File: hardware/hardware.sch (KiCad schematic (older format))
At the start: 18 parts, among them Q1 BUK7M33-60EX, U1 Teensy4.1_DEV-16771, U2 LT1910, U3 OKI, U4 OKI-78SR-3.3_1.5-W36H-C

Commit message: Board Review
Thermistor moved
Edit Ethernet
Find nichrome wire to be used before PDR
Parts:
- added C?: C_Small, symbol Device:C_Small
- added J?: RJ45_LED_Shielded, symbol Connector:RJ45_LED_Shielded
- added J?: 6P6C, symbol Connector:6P6C
- added TP? (x2): TestPoint, symbol Connector:TestPoint
- Conn1: symbol MRDT_Connectors:AndersonPP -> hardware-rescue:AndersonPP-MRDT_Connectors
- U2: symbol MRDT_ICs:LT1910 -> hardware-rescue:LT1910-MRDT_ICs
- U3: symbol MRDT_Devices:OKI -> hardware-rescue:OKI-MRDT_Devices
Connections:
- net labels added: EthernetMadness
- wire segments 84 -> 108
- no-connect marks 51 -> 56
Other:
- note removed: "A17 / A16 = TH1 / (TH1 + Nichrome Resistance)"
- note removed: "ethernet connection to teensy"
- moved on the sheet: TH1
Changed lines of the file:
@@
 $EndDescr
 $Comp
-L MRDT_Connectors:AndersonPP Conn1
+L hardware-rescue:AndersonPP-MRDT_Connectors Conn1
 U 4 1 614D2045
 P 700 1600
@@
 $EndComp
 $Comp
-L MRDT_Connectors:AndersonPP Conn1
+L hardware-rescue:AndersonPP-MRDT_Connectors Conn1
 U 1 1 614D689F
 P 700 1000
@@
 	1200 2100 1200 1900
 $Comp
-L MRDT_ICs:LT1910 U2
+L hardware-rescue:LT1910-MRDT_ICs U2
 U 1 1 61539417
 P 2250 1350
@@
 Wire Wire Line
 	2650 2150 2650 2000
-$Comp
-L power:GND #PWR06
-U 1 1 61591C99
-P 5050 6700
-F 0 "#PWR06" H 5050 6450 50  0001 C CNN
-F 1 "GND" V 5055 6572 50  0000 R CNN
-F 2 "" H 5050 6700 50  0001 C CNN
-F 3 "" H 5050 6700 50  0001 C CNN
-	1    5050 6700
-	0    -1   -1   0
-$EndComp
-Wire Wire Line
-	5050 6700 4950 6700
 Wire Wire Line
 	1650 1100 2050 1100
-Connection ~ 3300 2000
 NoConn ~ 4850 3100
 NoConn ~ 4850 3200
@@
 L Device:Thermistor_NTC TH1
 U 1 1 615942DB
-P 6300 2350
-F 0 "TH1" V 6010 2350 50  0000 C CNN
-F 1 "Thermistor_NTC" V 6101 2350 50  0000 C CNN
-F 2 "" H 6300 2400 50  0001 C CNN
-F 3 "~" H 6300 2400 50  0001 C CNN
-	1    6300 2350
+P 5700 1950
+F 0 "TH1" V 5410 1950 50  0000 C CNN
+F 1 "Thermistor_NTC" V 5501 1950 50  0000 C CNN
+F 2 "" H 5700 2000 50  0001 C CNN
+F 3 "~" H 5700 2000 50  0001 C CNN
+	1    5700 1950
 	0    1    1    0
 $EndComp
 Wire Wire Line
-	3300 2000 3300 2350
-Text Notes 7000 2200 0    50   ~ 0
-nichrome connection point
-Wire Wire Line
 	5250 2600 1650 2600
 Wire Wire Line
@@
 Wire Wire Line
 	4950 6800 4950 6700
-Connection ~ 4950 6700
 Wire Wire Line
 	4950 6700 4850 6700
-Text Notes 1550 4100 0    50   ~ 0
-ethernet connection to teensy
-Wire Wire Line
-	3250 3900 1950 3900
-$Comp
-L MRDT_Devices:OKI U3
+$Comp
+L hardware-rescue:OKI-MRDT_Devices U3
 U 1 1 615CF578
 P 6800 3300
@@
 Wire Wire Line
 	7300 4850 7550 4850
-Wire Wire Line
-	3950 1950 5450 1950
 NoConn ~ 3250 5700
 $Comp
@@
 $EndComp
 Wire Wire Line
-	6450 2350 6650 2350
-Connection ~ 6650 2350
-Wire Wire Line
-	6650 2350 7450 2350
-Wire Wire Line
 	5250 4400 5250 2600
 Wire Wire Line
 	4850 4400 5250 4400
 Wire Wire Line
-	4850 5700 5450 5700
-Wire Wire Line
-	5450 1950 5450 5700
-Wire Wire Line
-	3300 2350 6150 2350
-Connection ~ 5450 1950
-Wire Wire Line
-	5450 1950 7150 1950
-Wire Wire Line
 	4850 5800 5650 5800
 Wire Wire Line
-	5650 5800 5650 2600
-Wire Wire Line
-	6650 2350 6650 2600
-Wire Wire Line
-	5650 2600 6650 2600
-Text Notes 6050 1850 0    47   ~ 0
-A17 / A16 = TH1 / (TH1 + Nichrome Resistance)
+	5650 5800 5650 2250
+Wire Wire Line
+	5650 2250 6650 2250
 $Comp
 L Device:Thermistor_NTC TH3
@@
 Wire Wire Line
 	1200 1500 1200 1600
+$Comp
+L Connector:TestPoint TP?
+U 1 1 6164E01B
+P 7150 1950
+F 0 "TP?" V 7104 2138 50  0000 L CNN
+F 1 "TestPoint" V 7195 2138 50  0000 L CNN
+F 2 "" H 7350 1950 50  0001 C CNN
+F 3 "~" H 7350 1950 50  0001 C CNN
+	1    7150 1950
+	0    1    1    0
+$EndComp
+$Comp
+L Connector:TestPoint TP?
+U 1 1 616506C1
+P 7450 2350
+F 0 "TP?" V 7404 2538 50  0000 L CNN
+F 1 "TestPoint" V 7495 2538 50  0000 L CNN
+F 2 "" H 7650 2350 50  0001 C CNN
+F 3 "~" H 7650 2350 50  0001 C CNN
+	1    7450 2350
+	0    1    1    0
+$EndComp
+$Comp
+L Connector:RJ45_LED_Shielded J?
+U 1 1 61651929
+P 1100 4550
+F 0 "J?" V 1054 5080 50  0000 L CNN
+F 1 "RJ45_LED_Shielded" V 1145 5080 50  0000 L CNN
+F 2 "" V 1100 4575 50  0001 C CNN
+F 3 "~" V 1100 4575 50  0001 C CNN
+	1    1100 4550
+	0    1    1    0
+$EndComp
+NoConn ~ 3250 3900
+$Comp
+L Connector:6P6C J?
+U 1 1 61663DF2
+P 1000 5750
+F 0 "J?" V 1103 6180 50  0000 L CNN
+F 1 "6P6C" V 1012 6180 50  0000 L CNN
+F 2 "" V 1000 5775 50  0001 C CNN
+F 3 "~" V 1000 5775 50  0001 C CNN
+	1    1000 5750
+	0    1    -1   0
+$EndComp
+Wire Wire Line
+	1300 4950 1300 5150
+Wire Wire Line
+	600  4550 600  4800
+$Comp
+L power:GND #PWR?
+U 1 1 6167F4AF
+P 600 4800
+F 0 "#PWR?" H 600 4550 50  0001 C CNN
+F 1 "GND" H 605 4627 50  0000 C CNN
+F 2 "" H 600 4800 50  0001 C CNN
+F 3 "" H 600 4800 50  0001 C CNN
+	1    600  4800
+	1    0    0    -1
+$EndComp
+$Comp
+L Device:C_Small C?
+U 1 1 616800CF
+P 1650 5150
+F 0 "C?" H 1742 5196 50  0000 L CNN
+F 1 "C_Small" H 1742 5105 50  0000 L CNN
+F 2 "" H 1650 5150 50  0001 C CNN
+F 3 "~" H 1650 5150 50  0001 C CNN
+	1    1650 5150
+	1    0    0    -1
+$EndComp
+Wire Wire Line
+	1300 5150 1200 5150
+Wire Wire Line
+	1650 5050 1650 5000
+Wire Wire Line
+	800  4950 800  5350
+Wire Wire Line
+	1000 5250 1000 5350
+Wire Wire Line
+	1200 5150 1200 5350
+Wire Wire Line
+	1300 5200 1300 5350
+Wire Wire Line
+	1000 5250 1500 5250
+Wire Wire Line
+	1650 5000 1200 5000
+Wire Wire Line
+	1200 5000 1200 4950
+Connection ~ 1200 5000
+Wire Wire Line
+	900  4950 900  5000
+Wire Wire Line
+	900  5000 1200 5000
+Wire Wire Line
+	1300 5200 1100 5200
+Wire Wire Line
+	1100 5200 1100 4950
+Wire Wire Line
+	900  5350 900  5050
+Wire Wire Line
+	900  5050 1000 5050
+Wire Wire Line
+	1000 5050 1000 4950
+Wire Wire Line
+	1100 5350 1100 5300
+Wire Wire Line
+	1100 5300 1850 5300
+Wire Wire Line
+	1850 5300 1850 4150
+Wire Wire Line
+	1850 4150 1500 4150
+Wire Wire Line
+	1400 4150 1400 4100
+Wire Wire Line
+	1400 4100 1950 4100
+Wire Wire Line
+	1950 4100 1950 5250
+Wire Wire Line
+	1950 5250 1650 5250
+Connection ~ 1650 5250
+Wire Wire Line
+	1500 4950 1500 5250
+Connection ~ 1500 5250
+Wire Wire Line
+	1500 5250 1650 5250
+NoConn ~ 1400 4950
+NoConn ~ 800  4150
+NoConn ~ 900  4150
+Wire Wire Line
+	3300 2350 3300 2000
+Connection ~ 3300 2000
+Wire Wire Line
+	3300 2350 7450 2350
+Wire Wire Line
+	6650 2250 6650 1950
+Connection ~ 6650 1950
+Wire Wire Line
+	6650 1950 7150 1950
+Text Label 700  4050 0    50   ~ 0
+EthernetMadness
+Wire Wire Line
+	3950 1950 5550 1950
+NoConn ~ 4850 5700
+$Comp
+L power:GND #PWR06
+U 1 1 61591C99
+P 4950 6950
+F 0 "#PWR06" H 4950 6700 50  0001 C CNN
+F 1 "GND" V 4955 6822 50  0000 R CNN
+F 2 "" H 4950 6950 50  0001 C CNN
+F 3 "" H 4950 6950 50  0001 C CNN
+	1    4950 6950
+	1    0    0    -1
+$EndComp
+Wire Wire Line
+	4950 6950 4950 6800
+Connection ~ 4950 6800
+Wire Wire Line
+	5850 1950 6650 1950
+Text Notes 7000 2200 0    50   ~ 0
+nichrome connection point
 $EndSCHEMATC

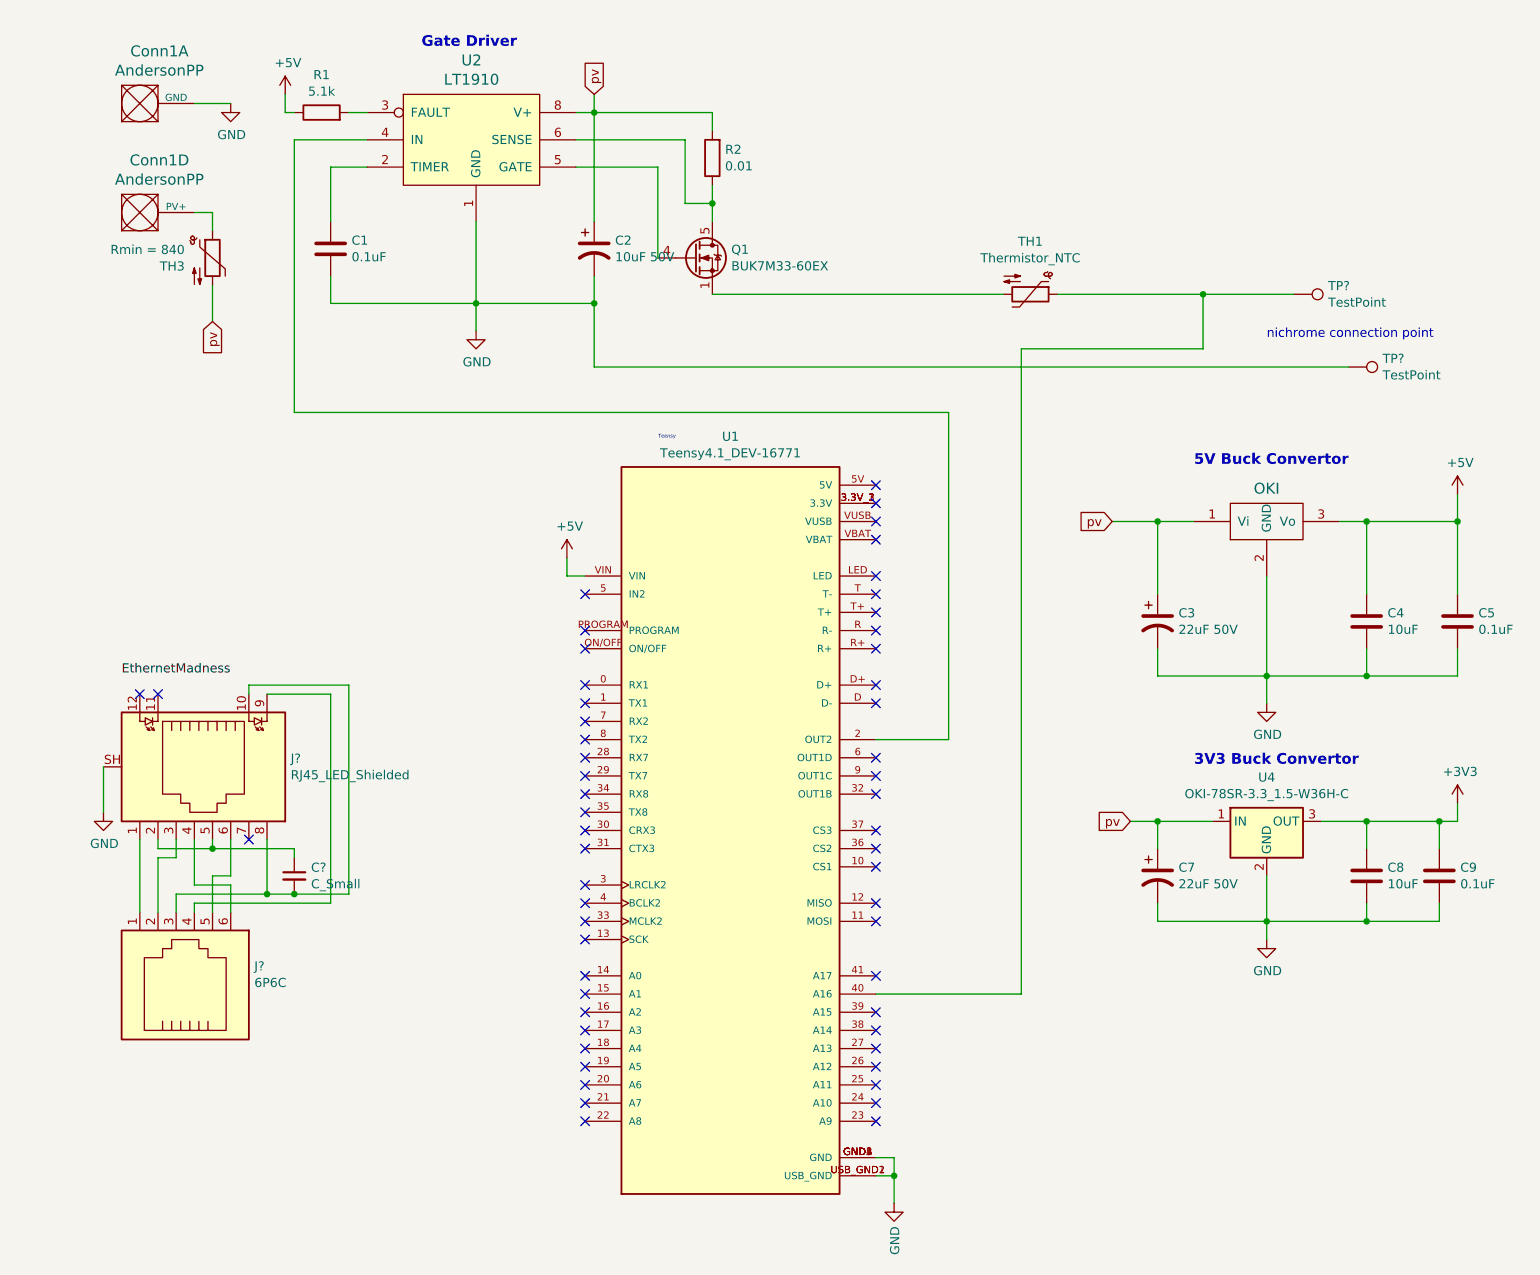
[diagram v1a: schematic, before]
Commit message: Cleaned up ethernet circuit wiring
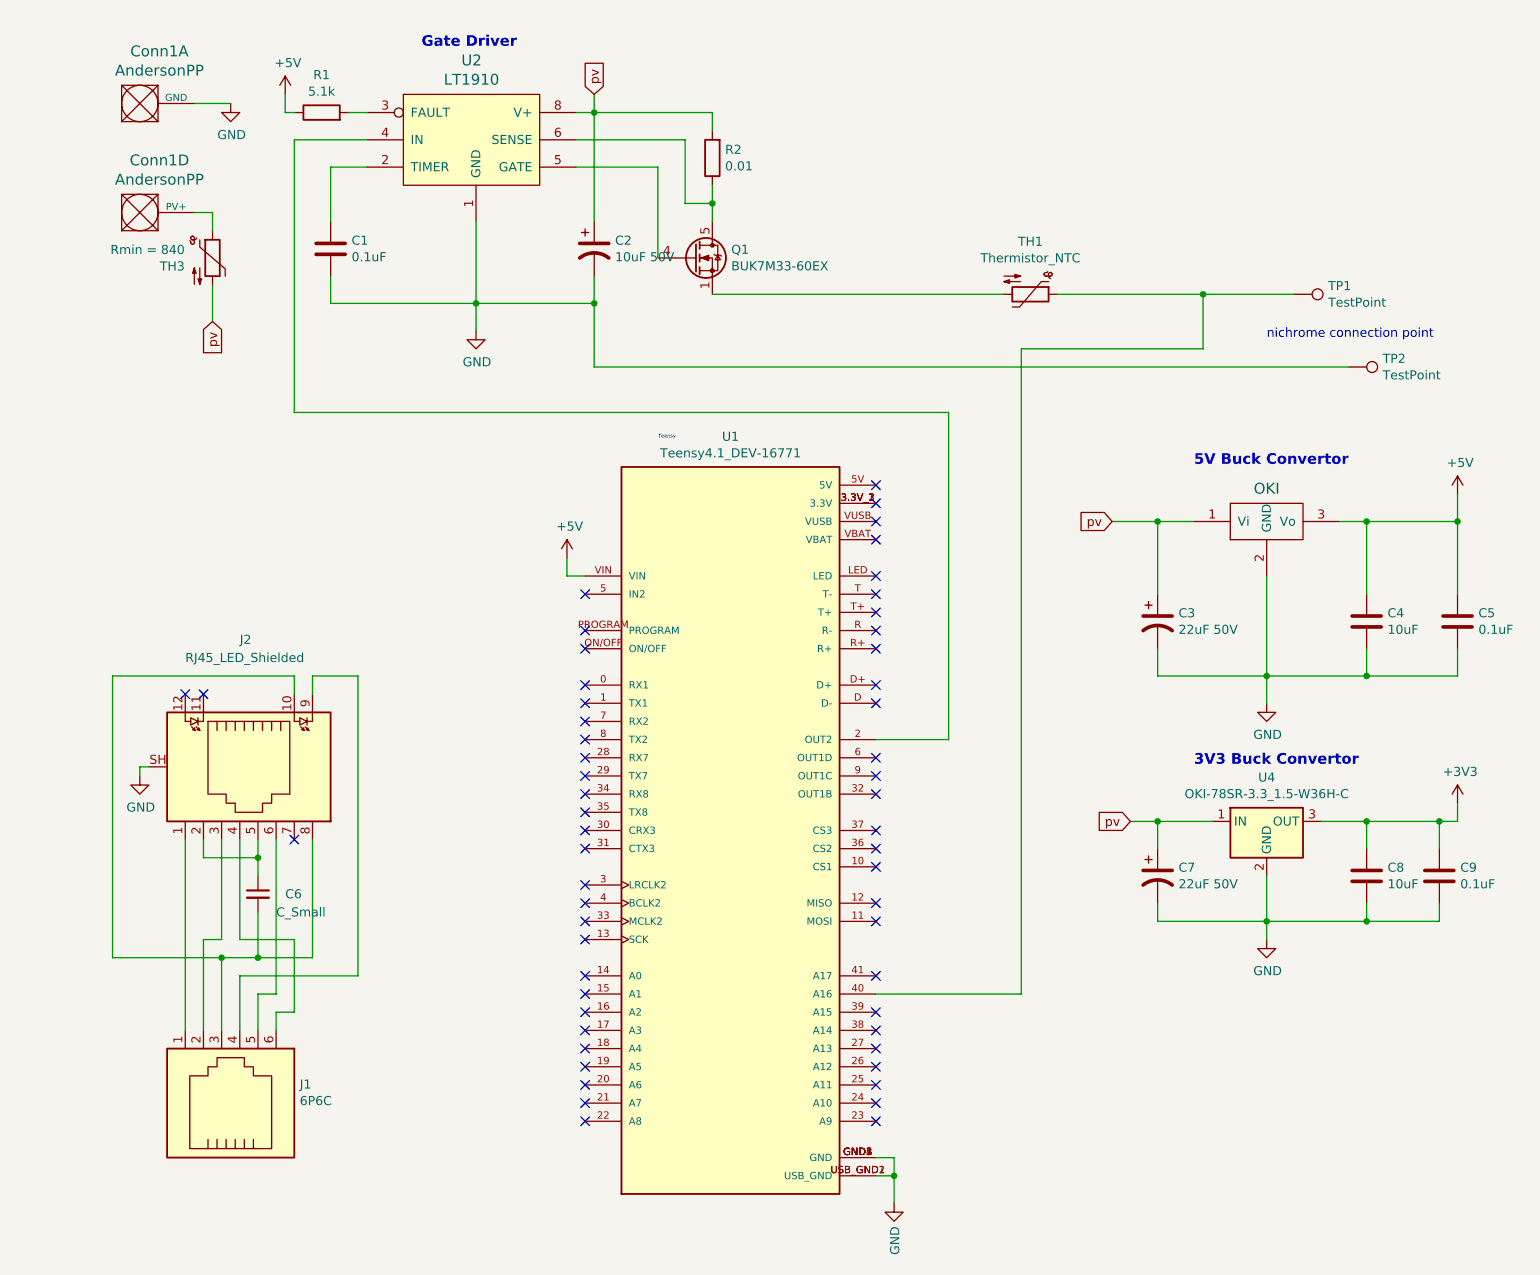
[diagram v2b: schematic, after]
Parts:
- removed C?: C_Small, symbol Device:C_Small
- added C6: C_Small, symbol Device:C_Small
- gave numbers to parts that had none: 4
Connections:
- net at J1.3, J2.10, J2.8: now also C6.2
- net at J2.2, J2.5: now also C6.1
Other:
- moved on the sheet: J1, J2
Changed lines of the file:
@@
 	1200 1500 1200 1600
 $Comp
-L Connector:TestPoint TP?
+L Connector:TestPoint TP1
 U 1 1 6164E01B
 P 7150 1950
-F 0 "TP?" V 7104 2138 50  0000 L CNN
+F 0 "TP1" V 7104 2138 50  0000 L CNN
 F 1 "TestPoint" V 7195 2138 50  0000 L CNN
 F 2 "" H 7350 1950 50  0001 C CNN
@@
 $EndComp
 $Comp
-L Connector:TestPoint TP?
+L Connector:TestPoint TP2
 U 1 1 616506C1
 P 7450 2350
-F 0 "TP?" V 7404 2538 50  0000 L CNN
+F 0 "TP2" V 7404 2538 50  0000 L CNN
 F 1 "TestPoint" V 7495 2538 50  0000 L CNN
 F 2 "" H 7650 2350 50  0001 C CNN
@@
 $EndComp
 $Comp
-L Connector:RJ45_LED_Shielded J?
+L Connector:RJ45_LED_Shielded J2
 U 1 1 61651929
-P 1100 4550
-F 0 "J?" V 1054 5080 50  0000 L CNN
-F 1 "RJ45_LED_Shielded" V 1145 5080 50  0000 L CNN
-F 2 "" V 1100 4575 50  0001 C CNN
-F 3 "~" V 1100 4575 50  0001 C CNN
-	1    1100 4550
+P 1350 4550
+F 0 "J2" V 650 4550 50  0000 L CNN
+F 1 "RJ45_LED_Shielded" V 750 4250 50  0000 L CNN
+F 2 "" V 1350 4575 50  0001 C CNN
+F 3 "~" V 1350 4575 50  0001 C CNN
+	1    1350 4550
 	0    1    1    0
 $EndComp
 NoConn ~ 3250 3900
 $Comp
-L Connector:6P6C J?
-U 1 1 61663DF2
-P 1000 5750
-F 0 "J?" V 1103 6180 50  0000 L CNN
-F 1 "6P6C" V 1012 6180 50  0000 L CNN
-F 2 "" V 1000 5775 50  0001 C CNN
-F 3 "~" V 1000 5775 50  0001 C CNN
-	1    1000 5750
-	0    1    -1   0
-$EndComp
-Wire Wire Line
-	1300 4950 1300 5150
-Wire Wire Line
-	600  4550 600  4800
-$Comp
-L power:GND #PWR?
+L power:GND #PWR01
 U 1 1 6167F4AF
-P 600 4800
-F 0 "#PWR?" H 600 4550 50  0001 C CNN
-F 1 "GND" H 605 4627 50  0000 C CNN
-F 2 "" H 600 4800 50  0001 C CNN
-F 3 "" H 600 4800 50  0001 C CNN
-	1    600  4800
-	1    0    0    -1
-$EndComp
-$Comp
-L Device:C_Small C?
-U 1 1 616800CF
-P 1650 5150
-F 0 "C?" H 1742 5196 50  0000 L CNN
-F 1 "C_Small" H 1742 5105 50  0000 L CNN
-F 2 "" H 1650 5150 50  0001 C CNN
-F 3 "~" H 1650 5150 50  0001 C CNN
-	1    1650 5150
+P 800 4600
+F 0 "#PWR01" H 800 4350 50  0001 C CNN
+F 1 "GND" H 805 4427 50  0000 C CNN
+F 2 "" H 800 4600 50  0001 C CNN
+F 3 "" H 800 4600 50  0001 C CNN
+	1    800  4600
 	1    0    0    -1
 $EndComp
 Wire Wire Line
-	1300 5150 1200 5150
-Wire Wire Line
-	1650 5050 1650 5000
-Wire Wire Line
-	800  4950 800  5350
-Wire Wire Line
-	1000 5250 1000 5350
-Wire Wire Line
-	1200 5150 1200 5350
-Wire Wire Line
-	1300 5200 1300 5350
-Wire Wire Line
-	1000 5250 1500 5250
-Wire Wire Line
-	1650 5000 1200 5000
-Wire Wire Line
-	1200 5000 1200 4950
-Connection ~ 1200 5000
-Wire Wire Line
-	900  4950 900  5000
-Wire Wire Line
-	900  5000 1200 5000
-Wire Wire Line
-	1300 5200 1100 5200
-Wire Wire Line
-	1100 5200 1100 4950
-Wire Wire Line
-	900  5350 900  5050
-Wire Wire Line
-	900  5050 1000 5050
-Wire Wire Line
-	1000 5050 1000 4950
-Wire Wire Line
-	1100 5350 1100 5300
-Wire Wire Line
-	1100 5300 1850 5300
-Wire Wire Line
-	1850 5300 1850 4150
-Wire Wire Line
-	1850 4150 1500 4150
-Wire Wire Line
-	1400 4150 1400 4100
-Wire Wire Line
-	1400 4100 1950 4100
-Wire Wire Line
-	1950 4100 1950 5250
-Wire Wire Line
-	1950 5250 1650 5250
-Connection ~ 1650 5250
-Wire Wire Line
-	1500 4950 1500 5250
-Connection ~ 1500 5250
-Wire Wire Line
-	1500 5250 1650 5250
-NoConn ~ 1400 4950
-NoConn ~ 800  4150
-NoConn ~ 900  4150
+	2000 4050 1750 4050
+NoConn ~ 1650 4950
+NoConn ~ 1050 4150
+NoConn ~ 1150 4150
 Wire Wire Line
 	3300 2350 3300 2000
@@
 Wire Wire Line
 	6650 1950 7150 1950
-Text Label 700  4050 0    50   ~ 0
-EthernetMadness
 Wire Wire Line
 	3950 1950 5550 1950
@@
 Text Notes 7000 2200 0    50   ~ 0
 nichrome connection point
+Wire Wire Line
+	800  4600 800  4550
+Wire Wire Line
+	800  4550 850  4550
+Wire Wire Line
+	1450 4950 1450 5050
+Wire Wire Line
+	1450 5050 1150 5050
+Wire Wire Line
+	1150 5050 1150 4950
+Wire Wire Line
+	1450 5050 1450 5150
+$Comp
+L Device:C_Small C6
+U 1 1 6167296B
+P 1450 5250
+F 0 "C6" H 1600 5250 50  0000 L CNN
+F 1 "C_Small" H 1550 5150 50  0000 L CNN
+F 2 "" H 1450 5250 50  0001 C CNN
+F 3 "~" H 1450 5250 50  0001 C CNN
+	1    1450 5250
+	1    0    0    -1
+$EndComp
+Connection ~ 1450 5050
+Wire Wire Line
+	1250 4950 1250 5500
+Wire Wire Line
+	1250 5500 1150 5500
+Wire Wire Line
+	1350 5700 2000 5700
+Wire Wire Line
+	1450 5800 1550 5800
+Wire Wire Line
+	1550 5800 1550 4950
+Wire Wire Line
+	1450 6000 1450 5800
+Wire Wire Line
+	1350 6000 1350 5700
+Wire Wire Line
+	1150 5500 1150 6000
+Wire Wire Line
+	1050 4950 1050 6000
+$Comp
+L Connector:6P6C J1
+U 1 1 61663DF2
+P 1250 6400
+F 0 "J1" V 1353 6830 50  0000 L CNN
+F 1 "6P6C" V 1262 6830 50  0000 L CNN
+F 2 "" V 1250 6425 50  0001 C CNN
+F 3 "~" V 1250 6425 50  0001 C CNN
+	1    1250 6400
+	0    1    -1   0
+$EndComp
+Wire Wire Line
+	1250 5600 1250 6000
+Wire Wire Line
+	1750 4950 1750 5600
+Connection ~ 1450 5600
+Wire Wire Line
+	1250 5600 1450 5600
+Wire Wire Line
+	1450 5600 1450 5350
+Wire Wire Line
+	1450 5600 1750 5600
+Wire Wire Line
+	1550 6000 1550 5900
+Wire Wire Line
+	1550 5900 1650 5900
+Wire Wire Line
+	1650 5900 1650 5500
+Wire Wire Line
+	1650 5500 1350 5500
+Wire Wire Line
+	1350 5500 1350 4950
+Wire Wire Line
+	1250 5600 650  5600
+Wire Wire Line
+	650  5600 650  4050
+Wire Wire Line
+	650  4050 1650 4050
+Wire Wire Line
+	1650 4050 1650 4150
+Connection ~ 1250 5600
+Wire Wire Line
+	2000 4050 2000 5700
+Wire Wire Line
+	1750 4050 1750 4150
 $EndSCHEMATC
